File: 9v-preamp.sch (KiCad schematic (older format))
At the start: 35 parts, among them J1 GND, J2 MJ-3536, J3 Conn_01x01_Female, J4 Conn_01x01_Female, J5 Conn_01x01_Female, J6 Conn_01x01_Female, J7 Conn_01x01_Female, J8 Conn_01x01_Female, J9 Conn_01x01_Female, SW1 TE6-1A-DC-1-PB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

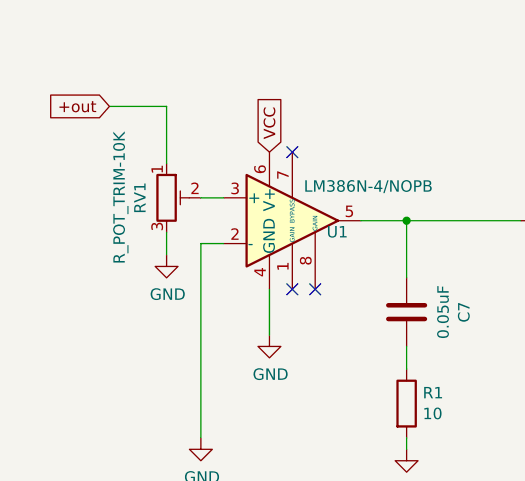
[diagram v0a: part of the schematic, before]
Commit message: Add files via upload
updated files, turned U1 around so It faces the same way as U2.
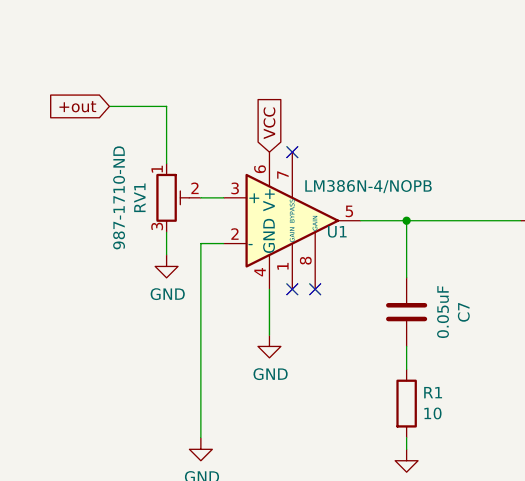
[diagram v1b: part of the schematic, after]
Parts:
- RV1: value R_POT_TRIM-10K -> 987-1710-ND
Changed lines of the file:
@@
 P 1700 1300
 F 0 "RV1" V 1585 1300 50  0000 C CNN
-F 1 "R_POT_TRIM-10K" V 1494 1300 50  0000 C CNN
+F 1 "987-1710-ND" V 1494 1300 50  0000 C CNN
 F 2 "Connector_PinHeader_2.54mm:PinHeader_1x03_P2.54mm_Vertical" H 1700 1300 50  0001 C CNN
 F 3 "~" H 1700 1300 50  0001 C CNN

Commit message: Add files via upload
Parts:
- D1: value 2339-TLM-87G-930-S-ND -> L20697-ND
- SW1: value TE6-1A-DC-1-PB -> 451-1158-ND
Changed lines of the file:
@@
 P 7100 800
 F 0 "SW1" H 7100 1035 50  0000 C CNN
-F 1 "TE6-1A-DC-1-PB" H 7100 944 50  0000 C CNN
+F 1 "451-1158-ND " H 7100 944 50  0000 C CNN
 F 2 "Connector_PinHeader_2.00mm:PinHeader_2x01_P2.00mm_Vertical" H 7100 800 50  0001 C CNN
 F 3 "~" H 7100 800 50  0001 C CNN
@@
 P 8850 1650
 F 0 "D1" V 8889 1532 50  0000 R CNN
-F 1 "2339-TLM-87G-930-S-ND" V 8798 1532 50  0000 R CNN
+F 1 "L20697-ND " V 8798 1532 50  0000 R CNN
 F 2 "LED_THT:LED_D2.0mm_W4.8mm_H2.5mm_FlatTop" H 8850 1650 50  0001 C CNN
 F 3 "~" H 8850 1650 50  0001 C CNN

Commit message: Add files via upload
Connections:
- net V- is gone; now on net GND: U2.4 (V-)
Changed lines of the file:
@@
 Text Notes 1050 5750 0    50   ~ 0
 TO SHIELD
+Text GLabel 3400 5400 3    50   Input ~ 0
+V-
 $EndSCHEMATC

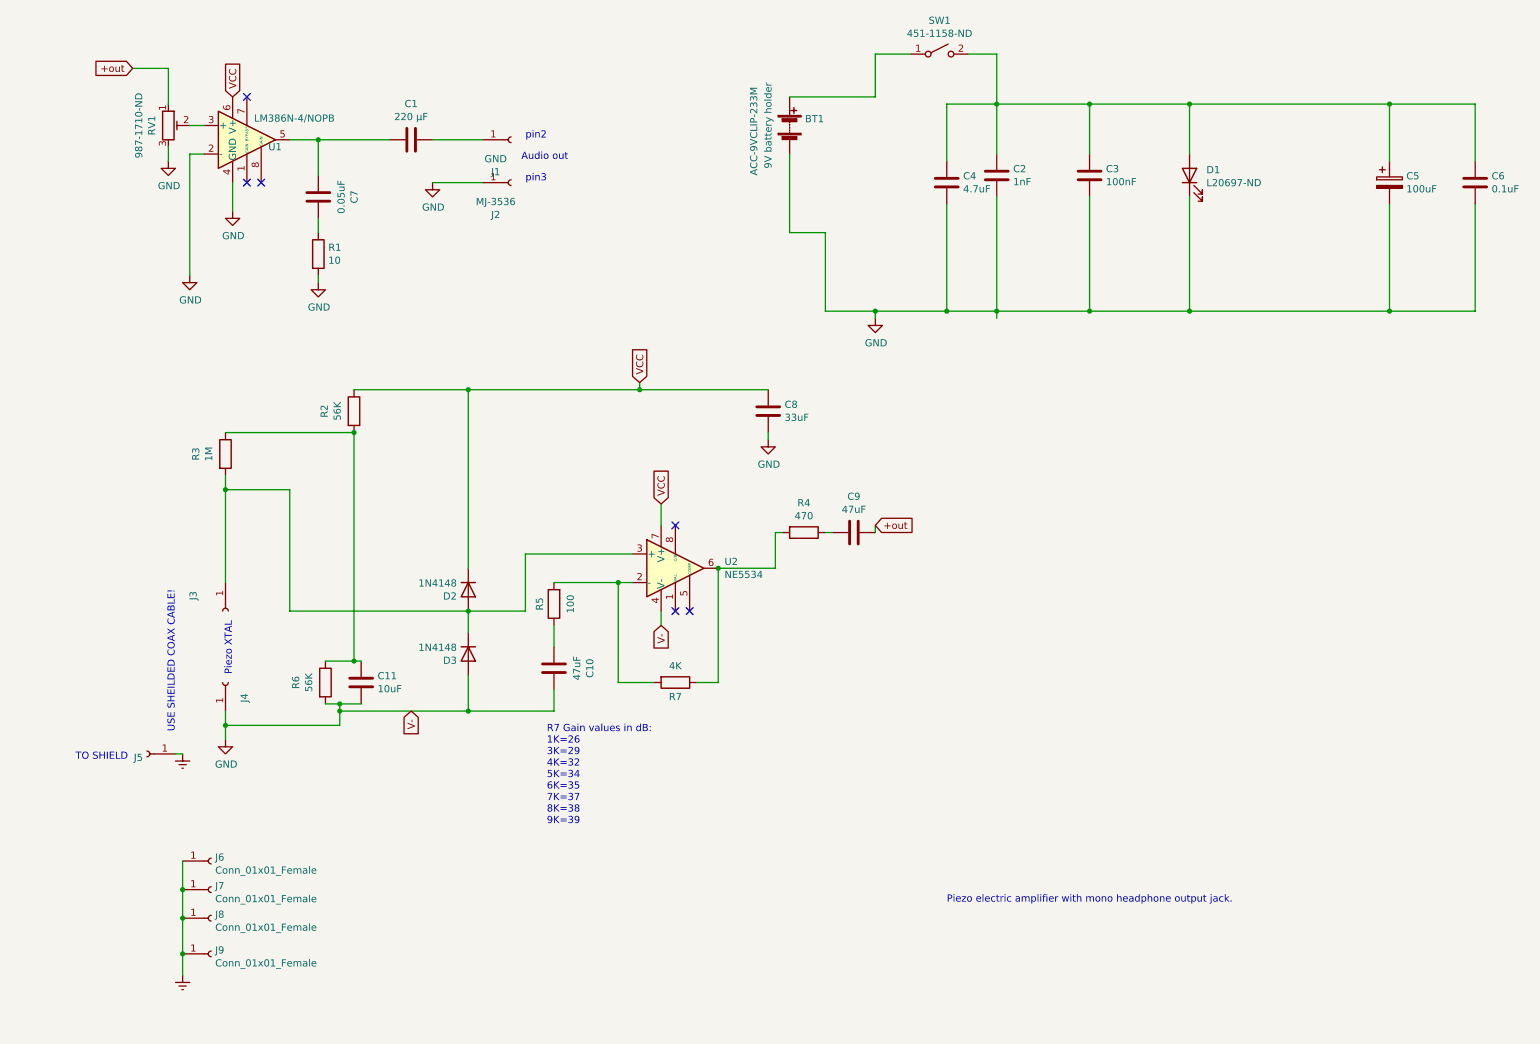
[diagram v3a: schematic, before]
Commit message: Add files via upload
corrected missing connection to VCC.
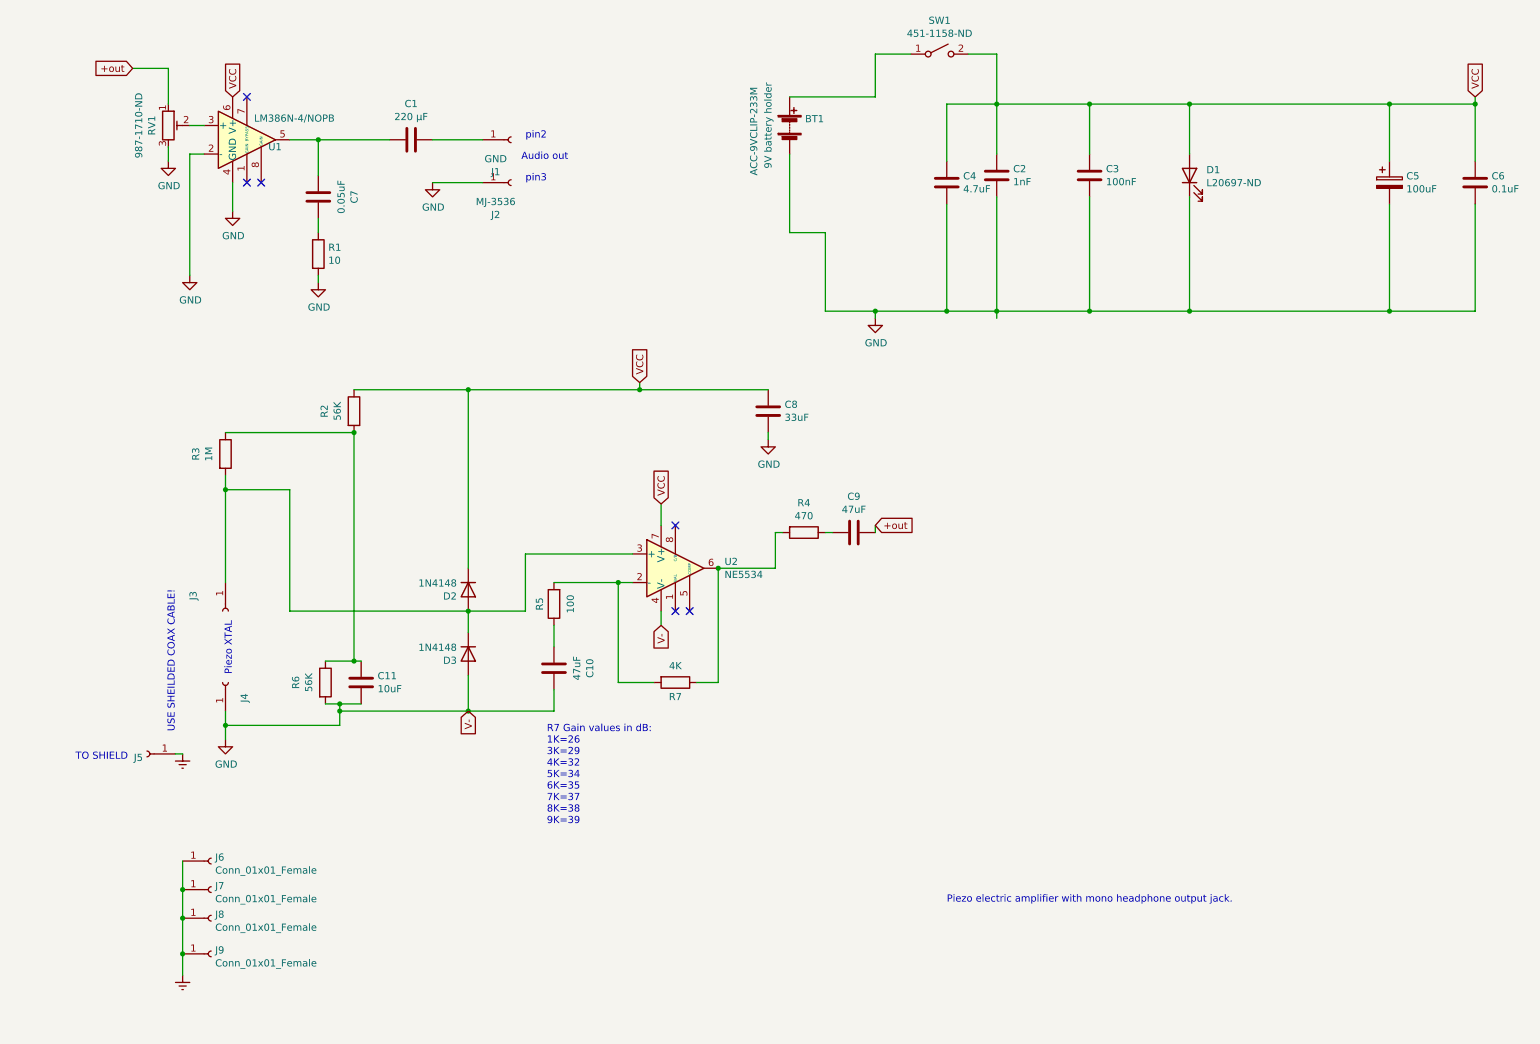
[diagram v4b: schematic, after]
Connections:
- net VCC: now also C2.2, C3.2, C4.1, C5.1, C6.2, D1.2 (A), SW1.2 (B)
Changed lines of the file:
@@
 Text Notes 1050 5750 0    50   ~ 0
 TO SHIELD
-Text GLabel 3400 5400 3    50   Input ~ 0
+Text GLabel 3800 5400 3    50   Input ~ 0
 V-
+Text GLabel 10850 1100 1    50   Input ~ 0
+VCC
+Wire Wire Line
+	10850 1100 10850 1150
+Connection ~ 10850 1150
 $EndSCHEMATC

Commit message: Add files via upload
Added + and - marks on the LED solder connections, and pin 1 on the op amps.
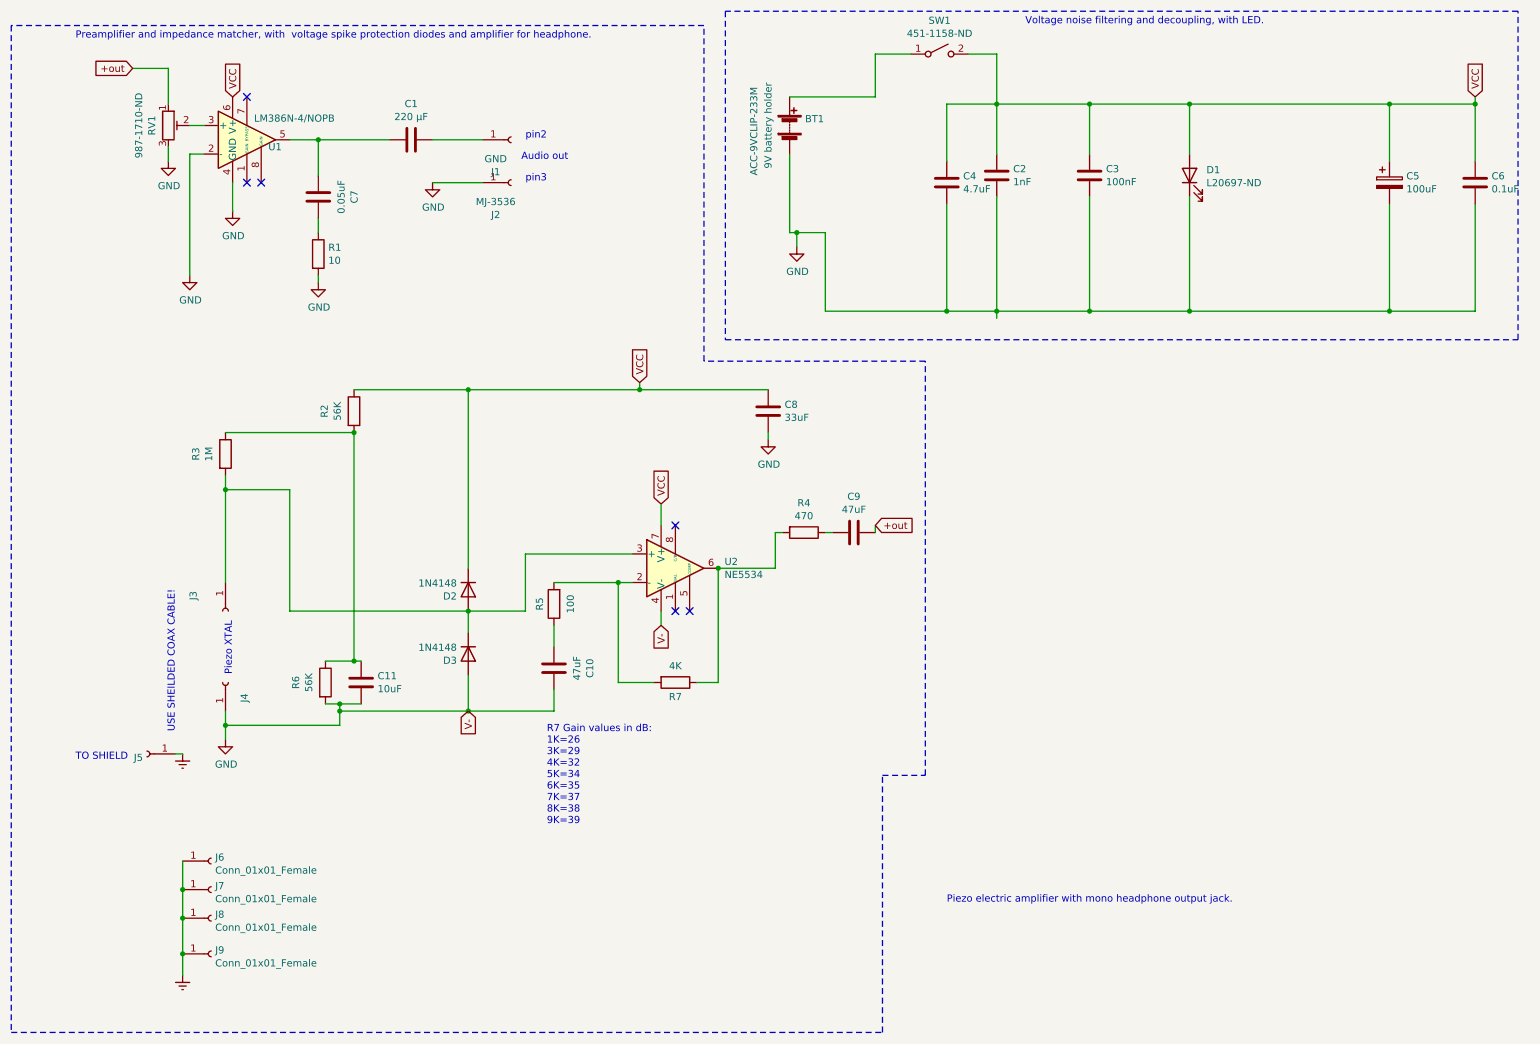
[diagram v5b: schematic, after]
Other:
- note added: "Preamplifier and impedance matcher, with voltage spike protection diodes and amplifier for headphone."
- note added: "Voltage noise filtering and decoupling, with LED."
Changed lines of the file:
@@
 Audio out
-$Comp
-L Connector:Conn_01x01_Female J6
-U 1 1 60C33F4A
-P 2000 6450
-F 0 "J6" H 2028 6476 50  0000 L CNN
-F 1 "Conn_01x01_Female" H 2028 6385 50  0000 L CNN
-F 2 "MountingHole:MountingHole_2.2mm_M2_DIN965_Pad" H 2000 6450 50  0001 C CNN
-F 3 "~" H 2000 6450 50  0001 C CNN
-	1    2000 6450
-	1    0    0    -1
-$EndComp
-$Comp
-L Connector:Conn_01x01_Female J7
-U 1 1 60C346FD
-P 2000 6650
-F 0 "J7" H 2028 6676 50  0000 L CNN
-F 1 "Conn_01x01_Female" H 2028 6585 50  0000 L CNN
-F 2 "MountingHole:MountingHole_2.2mm_M2_DIN965_Pad" H 2000 6650 50  0001 C CNN
-F 3 "~" H 2000 6650 50  0001 C CNN
-	1    2000 6650
-	1    0    0    -1
-$EndComp
-$Comp
-L Connector:Conn_01x01_Female J8
-U 1 1 60C34BAC
-P 2000 6850
-F 0 "J8" H 2028 6876 50  0000 L CNN
-F 1 "Conn_01x01_Female" H 2028 6785 50  0000 L CNN
-F 2 "MountingHole:MountingHole_2.2mm_M2_DIN965_Pad" H 2000 6850 50  0001 C CNN
-F 3 "~" H 2000 6850 50  0001 C CNN
-	1    2000 6850
-	1    0    0    -1
-$EndComp
-$Comp
-L Connector:Conn_01x01_Female J9
-U 1 1 60C36D7A
-P 2000 7100
-F 0 "J9" H 2028 7126 50  0000 L CNN
-F 1 "Conn_01x01_Female" H 2028 7035 50  0000 L CNN
-F 2 "MountingHole:MountingHole_2.2mm_M2_DIN965_Pad" H 2000 7100 50  0001 C CNN
-F 3 "~" H 2000 7100 50  0001 C CNN
-	1    2000 7100
-	1    0    0    -1
-$EndComp
 $Comp
 L Device:C C4
@@
 	6300 2050 6300 2600
 Wire Wire Line
-	6300 2600 6650 2600
-Wire Wire Line
-	6300 2050 6050 2050
+	6300 2050 6100 2050
 Wire Wire Line
 	7500 2600 7500 2650
@@
 L power:GND #PWR06
 U 1 1 60D1FD91
-P 6650 2650
-F 0 "#PWR06" H 6650 2400 50  0001 C CNN
-F 1 "GND" H 6655 2477 50  0000 C CNN
-F 2 "" H 6650 2650 50  0001 C CNN
-F 3 "" H 6650 2650 50  0001 C CNN
-	1    6650 2650
-	1    0    0    -1
-$EndComp
-Wire Wire Line
-	6650 2650 6650 2600
-Connection ~ 6650 2600
+P 6100 2150
+F 0 "#PWR06" H 6100 1900 50  0001 C CNN
+F 1 "GND" H 6105 1977 50  0000 C CNN
+F 2 "" H 6100 2150 50  0001 C CNN
+F 3 "" H 6100 2150 50  0001 C CNN
+	1    6100 2150
+	1    0    0    -1
+$EndComp
 Wire Wire Line
 	6650 1100 6650 800
@@
 Wire Wire Line
 	8850 1150 8850 1500
-Wire Wire Line
-	1800 6450 1800 6650
-Wire Wire Line
-	1800 6650 1800 6850
-Connection ~ 1800 6650
-Wire Wire Line
-	1800 6850 1800 7100
-Connection ~ 1800 6850
-$Comp
-L power:Earth #PWR09
-U 1 1 60D710DF
-P 1800 7250
-F 0 "#PWR09" H 1800 7000 50  0001 C CNN
-F 1 "Earth" H 1800 7100 50  0001 C CNN
-F 2 "" H 1800 7250 50  0001 C CNN
-F 3 "~" H 1800 7250 50  0001 C CNN
-	1    1800 7250
-	1    0    0    -1
-$EndComp
-Wire Wire Line
-	1800 7250 1800 7100
-Connection ~ 1800 7100
 $Comp
 L Amplifier_Audio:LM386 U1
@@
 	7500 800  7300 800
 Connection ~ 7500 1150
-Wire Wire Line
-	6650 2600 7150 2600
 $Comp
 L Device:C C9
@@
 	10850 1100 10850 1150
 Connection ~ 10850 1150
+Wire Notes Line
+	5600 500  5600 2800
+Wire Notes Line
+	5600 2800 11150 2800
+Wire Notes Line
+	11150 2800 11150 500
+Wire Notes Line
+	11150 500  5600 500
+Text Notes 7700 600  0    50   ~ 0
+Voltage noise filtering and decoupling, with LED.
+Connection ~ 1800 7100
+Wire Wire Line
+	1800 7250 1800 7100
+$Comp
+L power:Earth #PWR09
+U 1 1 60D710DF
+P 1800 7250
+F 0 "#PWR09" H 1800 7000 50  0001 C CNN
+F 1 "Earth" H 1800 7100 50  0001 C CNN
+F 2 "" H 1800 7250 50  0001 C CNN
+F 3 "~" H 1800 7250 50  0001 C CNN
+	1    1800 7250
+	1    0    0    -1
+$EndComp
+Connection ~ 1800 6850
+Wire Wire Line
+	1800 6850 1800 7100
+Connection ~ 1800 6650
+Wire Wire Line
+	1800 6650 1800 6850
+Wire Wire Line
+	1800 6450 1800 6650
+$Comp
+L Connector:Conn_01x01_Female J9
+U 1 1 60C36D7A
+P 2000 7100
+F 0 "J9" H 2028 7126 50  0000 L CNN
+F 1 "Conn_01x01_Female" H 2028 7035 50  0000 L CNN
+F 2 "MountingHole:MountingHole_2.2mm_M2_DIN965_Pad" H 2000 7100 50  0001 C CNN
+F 3 "~" H 2000 7100 50  0001 C CNN
+	1    2000 7100
+	1    0    0    -1
+$EndComp
+$Comp
+L Connector:Conn_01x01_Female J8
+U 1 1 60C34BAC
+P 2000 6850
+F 0 "J8" H 2028 6876 50  0000 L CNN
+F 1 "Conn_01x01_Female" H 2028 6785 50  0000 L CNN
+F 2 "MountingHole:MountingHole_2.2mm_M2_DIN965_Pad" H 2000 6850 50  0001 C CNN
+F 3 "~" H 2000 6850 50  0001 C CNN
+	1    2000 6850
+	1    0    0    -1
+$EndComp
+$Comp
+L Connector:Conn_01x01_Female J7
+U 1 1 60C346FD
+P 2000 6650
+F 0 "J7" H 2028 6676 50  0000 L CNN
+F 1 "Conn_01x01_Female" H 2028 6585 50  0000 L CNN
+F 2 "MountingHole:MountingHole_2.2mm_M2_DIN965_Pad" H 2000 6650 50  0001 C CNN
+F 3 "~" H 2000 6650 50  0001 C CNN
+	1    2000 6650
+	1    0    0    -1
+$EndComp
+$Comp
+L Connector:Conn_01x01_Female J6
+U 1 1 60C33F4A
+P 2000 6450
+F 0 "J6" H 2028 6476 50  0000 L CNN
+F 1 "Conn_01x01_Female" H 2028 6385 50  0000 L CNN
+F 2 "MountingHole:MountingHole_2.2mm_M2_DIN965_Pad" H 2000 6450 50  0001 C CNN
+F 3 "~" H 2000 6450 50  0001 C CNN
+	1    2000 6450
+	1    0    0    -1
+$EndComp
+Wire Notes Line
+	600  600  600  7650
+Wire Notes Line
+	600  7650 6700 7650
+Wire Notes Line
+	6700 7650 6700 5850
+Wire Notes Line
+	6700 5850 7000 5850
+Wire Notes Line
+	7000 5850 7000 2950
+Wire Notes Line
+	7000 2950 5450 2950
+Wire Notes Line
+	5450 2950 5450 600
+Wire Notes Line
+	5450 600  600  600
+Text Notes 1050 700  0    50   ~ 0
+Preamplifier and impedance matcher, with  voltage spike protection diodes and amplifier for headphone.
+Wire Wire Line
+	6300 2600 7150 2600
+Wire Wire Line
+	6100 2150 6100 2050
+Connection ~ 6100 2050
+Wire Wire Line
+	6100 2050 6050 2050
 $EndSCHEMATC

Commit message: Add files via upload
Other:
- note added: "SLEEVE"
- note added: "TIP"
- note removed: "pin2"
- note removed: "pin3"
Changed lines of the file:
@@
 	1    0    0    -1
 $EndComp
-Text Notes 4350 1400 2    50   ~ 0
-pin2
-Text Notes 4350 1700 2    50   ~ 0
-pin3
+Text Notes 4250 1450 2    50   ~ 0
+TIP
+Text Notes 4400 1750 2    50   ~ 0
+SLEEVE
 Wire Wire Line
 	1850 1500 1950 1500
